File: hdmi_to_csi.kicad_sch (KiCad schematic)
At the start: 4 parts, among them P1 22P_FPC, U7 TC358743XBG_EL_NOK, X2 27MHz

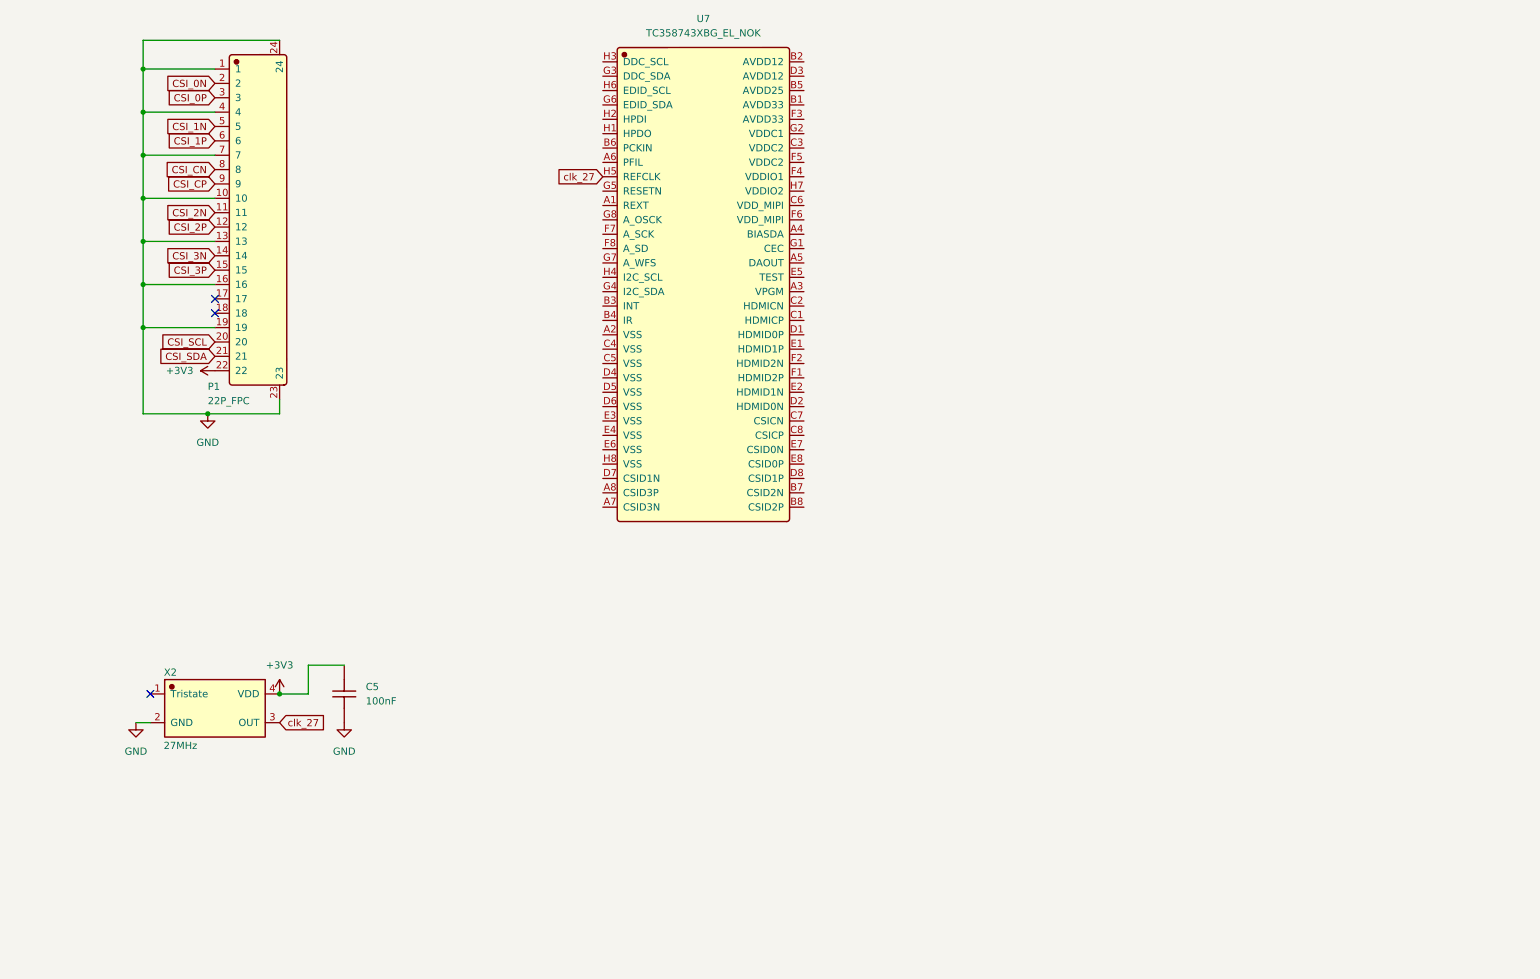
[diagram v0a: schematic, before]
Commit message: HDMI->CSI adapter v0.1
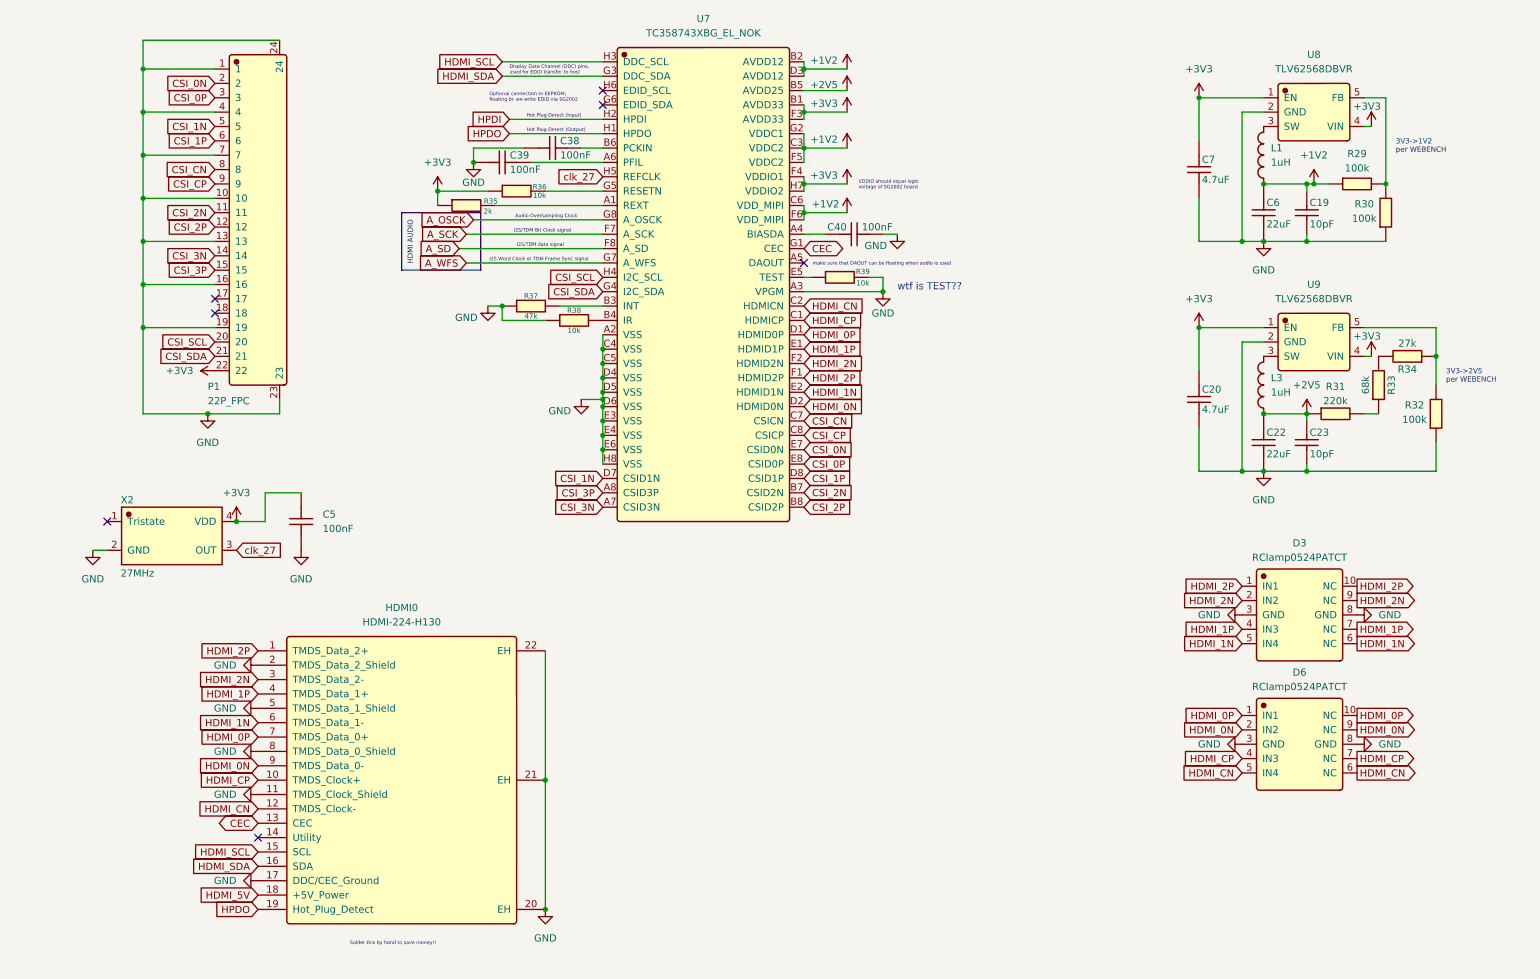
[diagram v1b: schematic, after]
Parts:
- added C19, C23: 10pF, Capacitor_SMD:C_0603_1608Metric, symbol JLCImport:CL10C100JB8NNNC
- added C20, C7: 4.7uF, Capacitor_SMD:C_0603_1608Metric, symbol JLCImport:CL10A475KO8NNNC
- added C22, C6: 22uF, Capacitor_SMD:C_0603_1608Metric, symbol JLCImport:CL10A226MQ8NRNC
- added C38, C39, C40: 100nF, Capacitor_SMD:C_0402_1005Metric, symbol JLCImport:CL05B104KB54PNC
- added D3, D6: RClamp0524PATCT, JLCImport:RClamp0524PATCT, symbol JLCImport:RClamp0524PATCT
- added HDMI0: HDMI-224-H130, JLCImport:HDMI-224-H130, symbol JLCImport:HDMI-224-H130
- added L1, L3: 1uH, TerminalBlock_Phoenix:TerminalBlock_Phoenix_PTSM-0,5-2-2,5-V-SMD_1x02-1MP_P2.50mm_Vertical, symbol JLCImport:FTC252012S1R0MBCA
- added R29, R30, R32: 100k, Resistor_SMD:R_0402_1005Metric, symbol JLCImport:0402WGF1003TCE
- added R31: 220k, Resistor_SMD:R_0603_1608Metric, symbol JLCImport:0603WAF2203T5E
- added R33: 68k, Resistor_SMD:R_0603_1608Metric, symbol JLCImport:0603WAF6802T5E
- added R34: 27k, Resistor_SMD:R_0603_1608Metric, symbol JLCImport:0603WAF2702T5E
- added R35: 2k, Resistor_SMD:R_0603_1608Metric, symbol JLCImport:0603WAF2001T5E
- added R36, R38, R39: 10k, Resistor_SMD:R_0402_1005Metric, symbol JLCImport:0402WGF1002TCE
- added R37: 47k, Resistor_SMD:R_0402_1005Metric, symbol JLCImport:0402WGF4702TCE
- added U8, U9: TLV62568DBVR, JLCImport:TLV62568DBVR, symbol JLCImport:TLV62568DBVR
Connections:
- net +3V3: now also U7.B1 (AVDD33), U7.F3 (AVDD33), U7.F4 (VDDIO1), U7.H7 (VDDIO2), C20.2, C7.2, R35.1, R36.1, U8.1 (EN), U8.4 (VIN), U9.1 (EN), U9.4 (VIN)
- net CSI_0N: now also U7.E7 (CSID0N)
- net CSI_0P: now also U7.E8 (CSID0P)
- net CSI_1N: now also U7.D7 (CSID1N)
- net CSI_1P: now also U7.D8 (CSID1P)
- net CSI_2P: now also U7.B8 (CSID2P)
- net CSI_3N: now also U7.A7 (CSID3N)
- net CSI_3P: now also U7.A8 (CSID3P)
- net CSI_CN: now also U7.C7 (CSICN)
- net CSI_CP: now also U7.C8 (CSICP)
- net CSI_SCL: now also U7.H4 (I2C_SCL)
- net CSI_SDA: now also U7.G4 (I2C_SDA)
- net GND: now also U7.A2 (VSS), U7.A3 (VPGM), U7.C4 (VSS), U7.C5 (VSS), U7.D4 (VSS), U7.D5 (VSS), U7.D6 (VSS), U7.E3 (VSS), U7.E4 (VSS), U7.E6 (VSS), U7.H8 (VSS), C19.1, C20.1, C22.1, C23.1, C38.1, C39.1, C40.2, C6.1, C7.1, D3.3 (GND), D3.8 (GND), D6.3 (GND), D6.8 (GND), HDMI0.11 (TMDS_Clock_Shield), HDMI0.17 (DDC/CEC_Ground), HDMI0.2 (TMDS_Data_2_Shield), HDMI0.20 (EH), HDMI0.21 (EH), HDMI0.22 (EH), HDMI0.5 (TMDS_Data_1_Shield), HDMI0.8 (TMDS_Data_0_Shield), R30.1, R32.1, R37.1, R38.1, R39.2, U8.2 (GND), U9.2 (GND)
- net at U7.A1 (REXT): now also R35.2
- net at U7.A4 (BIASDA): now also C40.1
- net at U7.A6 (PFIL): now also C39.2
- net +1V2: now reaches U7.B2 (AVDD12)
- net +1V2: now also U7.C3 (VDDC2), U7.C6 (VDD_MIPI), U7.D3 (AVDD12), U7.F5 (VDDC2), U7.F6 (VDD_MIPI), U7.G2 (VDDC1), C19.2, C6.2, L1.1, R29.1
- net at U7.B3 (INT): now also R37.2
- net at U7.B4 (IR): now also R38.2
- net +2V5: now reaches U7.B5 (AVDD25)
- net +2V5: now also C22.2, C23.2, L3.1, R31.1
- net at U7.B6 (PCKIN): now also C38.2
- net HDMI_CP: now reaches U7.C1 (HDMICP)
- net HDMI_CP: now also D6.4 (IN3), D6.7 (NC), HDMI0.10 (TMDS_Clock+)
- net HDMI_CN: now reaches U7.C2 (HDMICN)
- net HDMI_CN: now also D6.5 (IN4), D6.6 (NC), HDMI0.12 (TMDS_Clock-)
- net HDMI_0P: now reaches U7.D1 (HDMID0P)
- net HDMI_0P: now also D6.1 (IN1), D6.10 (NC), HDMI0.7 (TMDS_Data_0+)
- net HDMI_0N: now reaches U7.D2 (HDMID0N)
- net HDMI_0N: now also D6.2 (IN2), D6.9 (NC), HDMI0.9 (TMDS_Data_0-)
- net HDMI_1P: now reaches U7.E1 (HDMID1P)
- net HDMI_1P: now also D3.4 (IN3), D3.7 (NC), HDMI0.4 (TMDS_Data_1+)
- net HDMI_1N: now reaches U7.E2 (HDMID1N)
- net HDMI_1N: now also D3.5 (IN4), D3.6 (NC), HDMI0.6 (TMDS_Data_1-)
- net at U7.E5 (TEST): now also R39.1
- net HDMI_2P: now reaches U7.F1 (HDMID2P)
- net HDMI_2P: now also D3.1 (IN1), D3.10 (NC), HDMI0.1 (TMDS_Data_2+)
- net HDMI_2N: now reaches U7.F2 (HDMID2N)
- net HDMI_2N: now also D3.2 (IN2), D3.9 (NC), HDMI0.3 (TMDS_Data_2-)
- net A_SCK: now reaches U7.F7 (A_SCK)
- net A_SD: now reaches U7.F8 (A_SD)
- net CEC: now reaches U7.G1 (CEC)
- net CEC: now also HDMI0.13 (CEC)
- net HDMI_SDA: now reaches U7.G3 (DDC_SDA)
- net HDMI_SDA: now also HDMI0.16 (SDA)
- net at U7.G5 (RESETN): now also R36.2
- net A_WFS: now reaches U7.G7 (A_WFS)
- net A_OSCK: now reaches U7.G8 (A_OSCK)
- net HPDO: now reaches U7.H1 (HPDO)
- net HPDO: now also HDMI0.19 (Hot_Plug_Detect)
- net HPDI: now reaches U7.H2 (HPDI)
- net HDMI_SCL: now reaches U7.H3 (DDC_SCL)
- net HDMI_SCL: now also HDMI0.15 (SCL)
- new net: L1.2, U8.3 (SW)
- new net: R32.2, R34.1, U9.5 (FB)
- new net: R33.2, R34.2
- new net: R29.2, R30.2, U8.5 (FB)
- new net: L3.2, U9.3 (SW)
- new net: R31.2, R33.1
- new net HDMI_5V: HDMI0.18 (+5V_Power)
- no-connect marks 3 -> 7
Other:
- note added: "3V3->1V2 per WEBENCH"
- note added: "3V3->2V5 per WEBENCH"
- note added: "Audio Oversampling Clock"
- note added: "Display Data Channel (DDC) pins, used for EDID transfer to host"
- note added: "HDMI AUDIO"
- note added: "Hot Plug Detect (Input)"
- note added: "Hot Plug Detect (Output)"
- note added: "I2S Word Clock or TDM Frame Sync signal"
- note added: "I2S/TDM Bit Clock signal"
- note added: "I2S/TDM data signal"
- note added: "Optional connection to EEPROM; floating bc we write EDID via SG2002"
- note added: "Solder this by hand to save money!!"
- note added: "VDDIO should equal logic voltage of SG2002 board"
- note added: "make sure that DAOUT can be floating when audio is used"
- note added: "wtf is TEST??"
- company: (none) -> Matthew Kong
- title: (none) -> Custom HDMI->CSI for SG2002 IPKVM
- moved on the sheet: C5, X2
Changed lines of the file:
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@@
 	(generator_version "10.0")
 	(paper "A4")
+	(title_block
+		(title "Custom HDMI->CSI for SG2002 IPKVM")
+		(company "Matthew Kong")
+	)

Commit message: Added bypass capacitors and pull up resistors to HDMI->CSI adapter
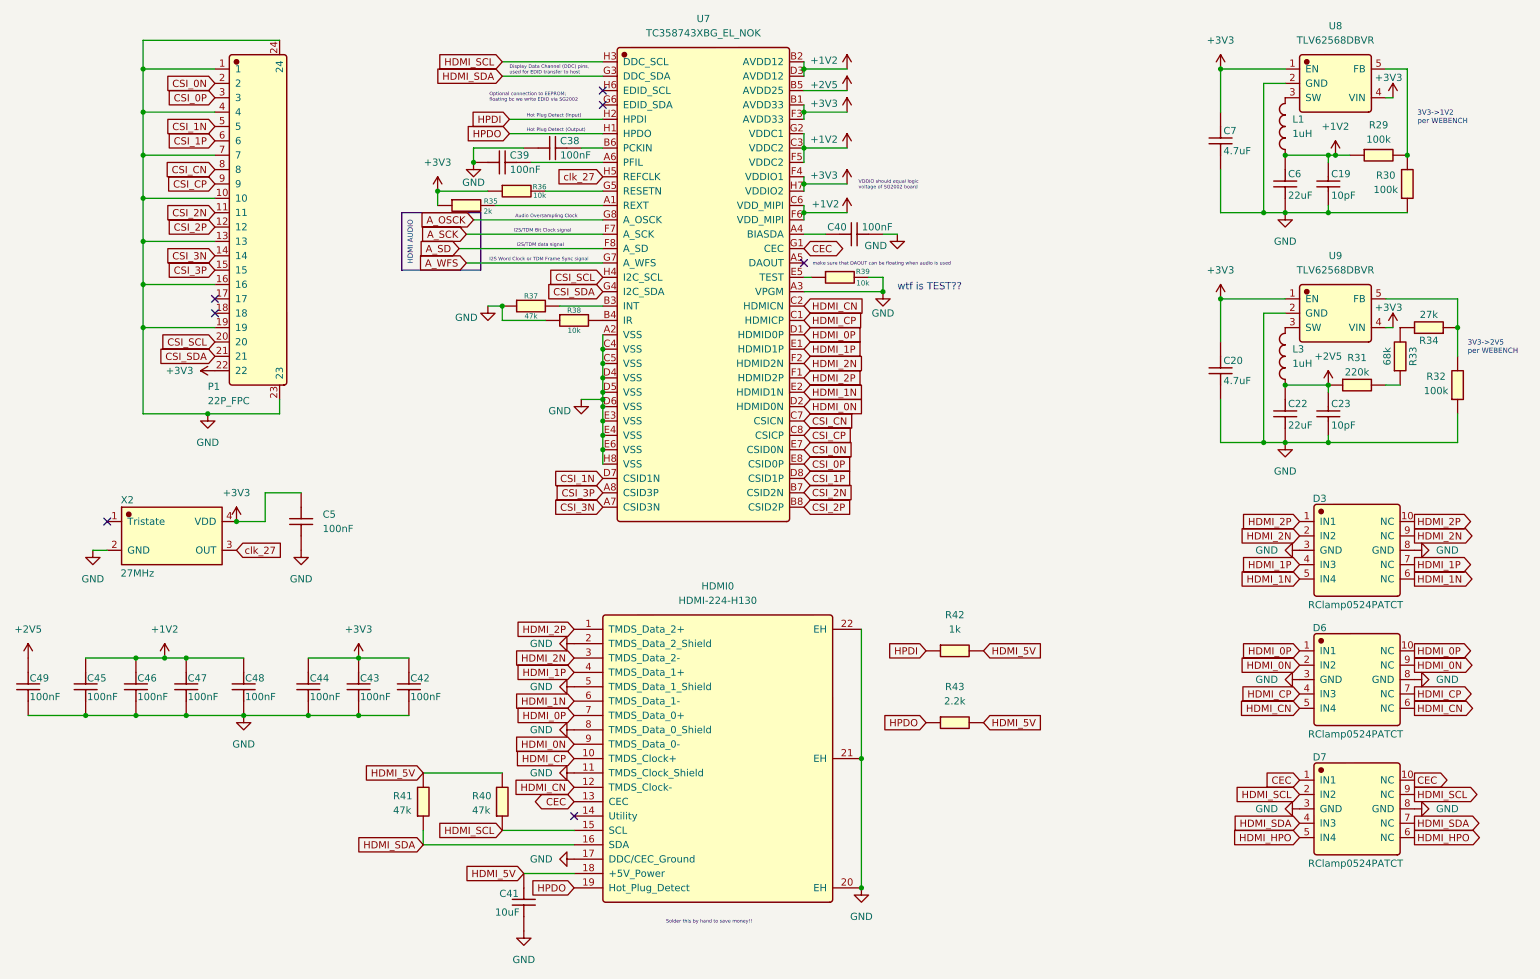
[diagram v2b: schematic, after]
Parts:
- added C41: 10uF, Capacitor_SMD:C_0603_1608Metric, symbol JLCImport:CL10A106KP8NNNC
- added C42, C43, C44, C45, C46, C47, C48, C49: 100nF, Capacitor_SMD:C_0402_1005Metric, symbol JLCImport:CL05B104KB54PNC
- added D7: RClamp0524PATCT, JLCImport:RClamp0524PATCT, symbol JLCImport:RClamp0524PATCT
- added R40, R41: 47k, Resistor_SMD:R_0402_1005Metric, symbol JLCImport:0402WGF4702TCE
- added R42: 1k, Resistor_SMD:R_0402_1005Metric, symbol JLCImport:0402WGF1001TCE
- added R43: 2.2k, Resistor_SMD:R_0402_1005Metric, symbol JLCImport:0402WGF2201TCE
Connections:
- net +1V2: now also C45.2, C46.2, C47.2, C48.2
- net +2V5: now also C49.2
- net +3V3: now also C42.2, C43.2, C44.2
- net CEC: now also D7.1 (IN1), D7.10 (NC)
- net GND: now also C41.1, C42.1, C43.1, C44.1, C45.1, C46.1, C47.1, C48.1, C49.1, D7.3 (GND), D7.8 (GND)
- net HDMI_5V: now also C41.2, R40.2, R41.2, R42.2, R43.2
- net HDMI_SCL: now also D7.2 (IN2), D7.9 (NC), R40.1
- net HDMI_SDA: now also D7.4 (IN3), D7.7 (NC), R41.1
- net HPDI: now also R42.1
- net HPDO: now also R43.1
- new net HDMI_HPO: D7.5 (IN4), D7.6 (NC)
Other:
- moved on the sheet: C19, C20, C22, C23, C6, C7, D3, D6, HDMI0, L1, L3, R29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
